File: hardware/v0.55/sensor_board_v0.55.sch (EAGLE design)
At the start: 58 parts, among them J3 USB-MICROB, J6 AVR_SPI_PRG_6PTH, U1 ATMEGA328P, U10 TSL2591, U2 SHT35, U3 OPA344, U5 FT231XS, U6 ADMP401, U7 RFM69HCW, U8 MCP1703CB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

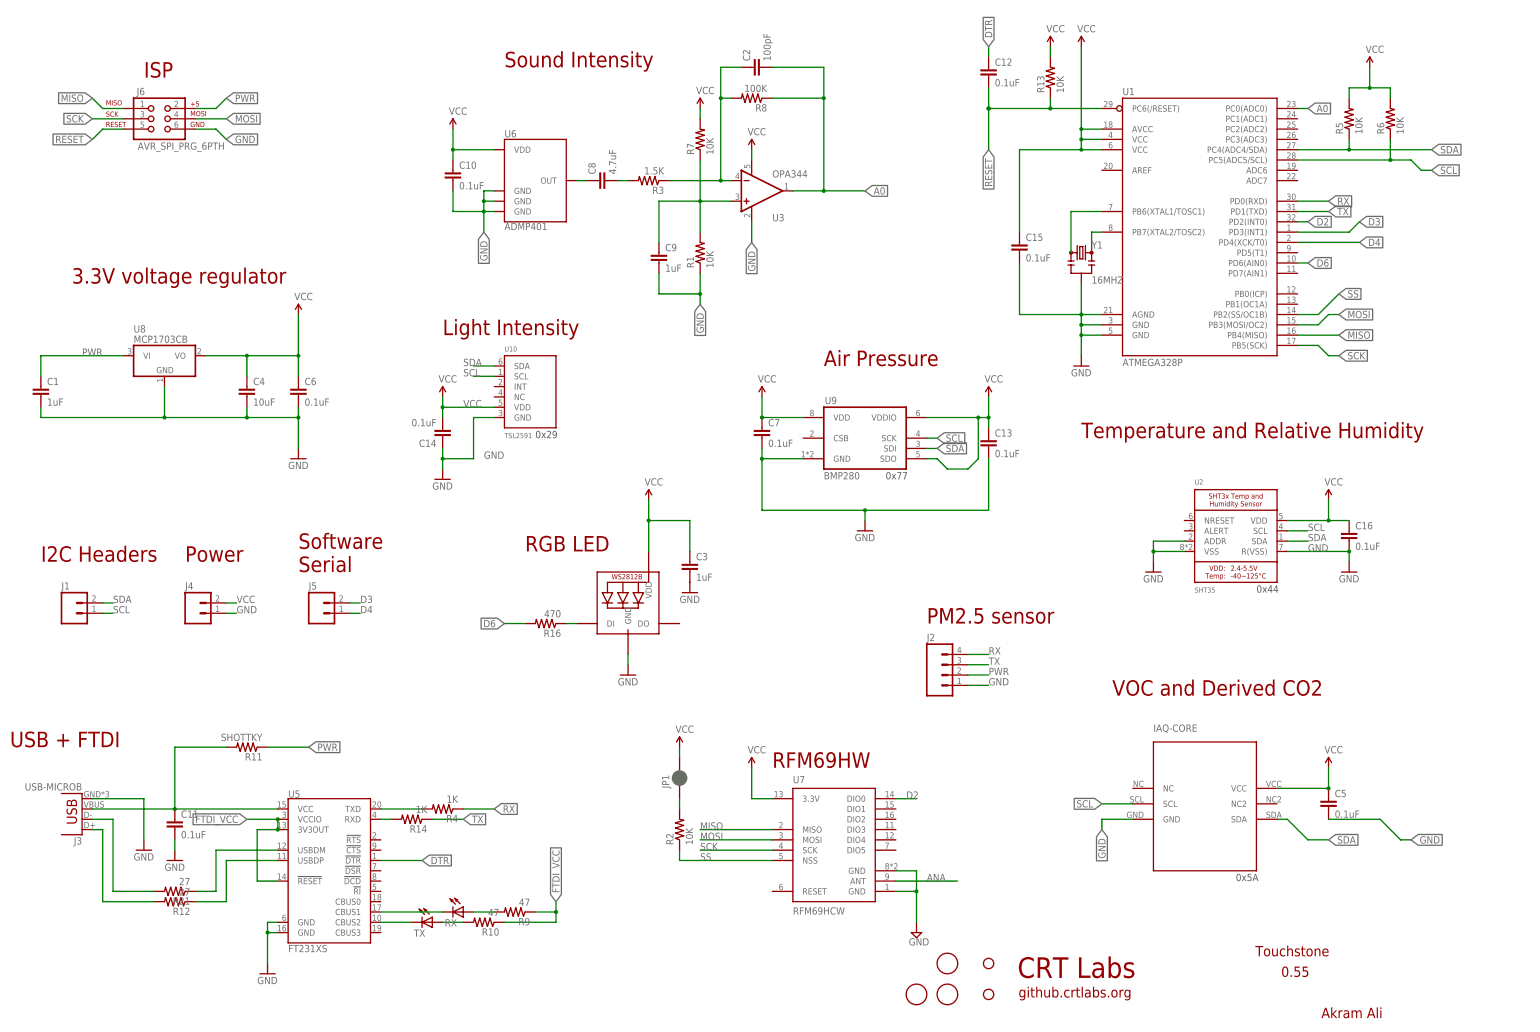
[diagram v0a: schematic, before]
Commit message: v0.55 - Major design update
- Added 2x5 header for PMS7003 PM sensor
- Moved microphone+amp circuitry to accomodate for the PM sensor header
- Removed UART and software serial breakout headers
- Moved voltage regulator circuitry in space created by removing UART
header
- Moved LED in space created by moving voltage regulator
- Moved light sensor to be in line with LED
- Rerouted several traces to accomodate for new design
- Some silkscreen adjustments
- Provided some more tolerance to the mounting holes
- Moved fiducial markers
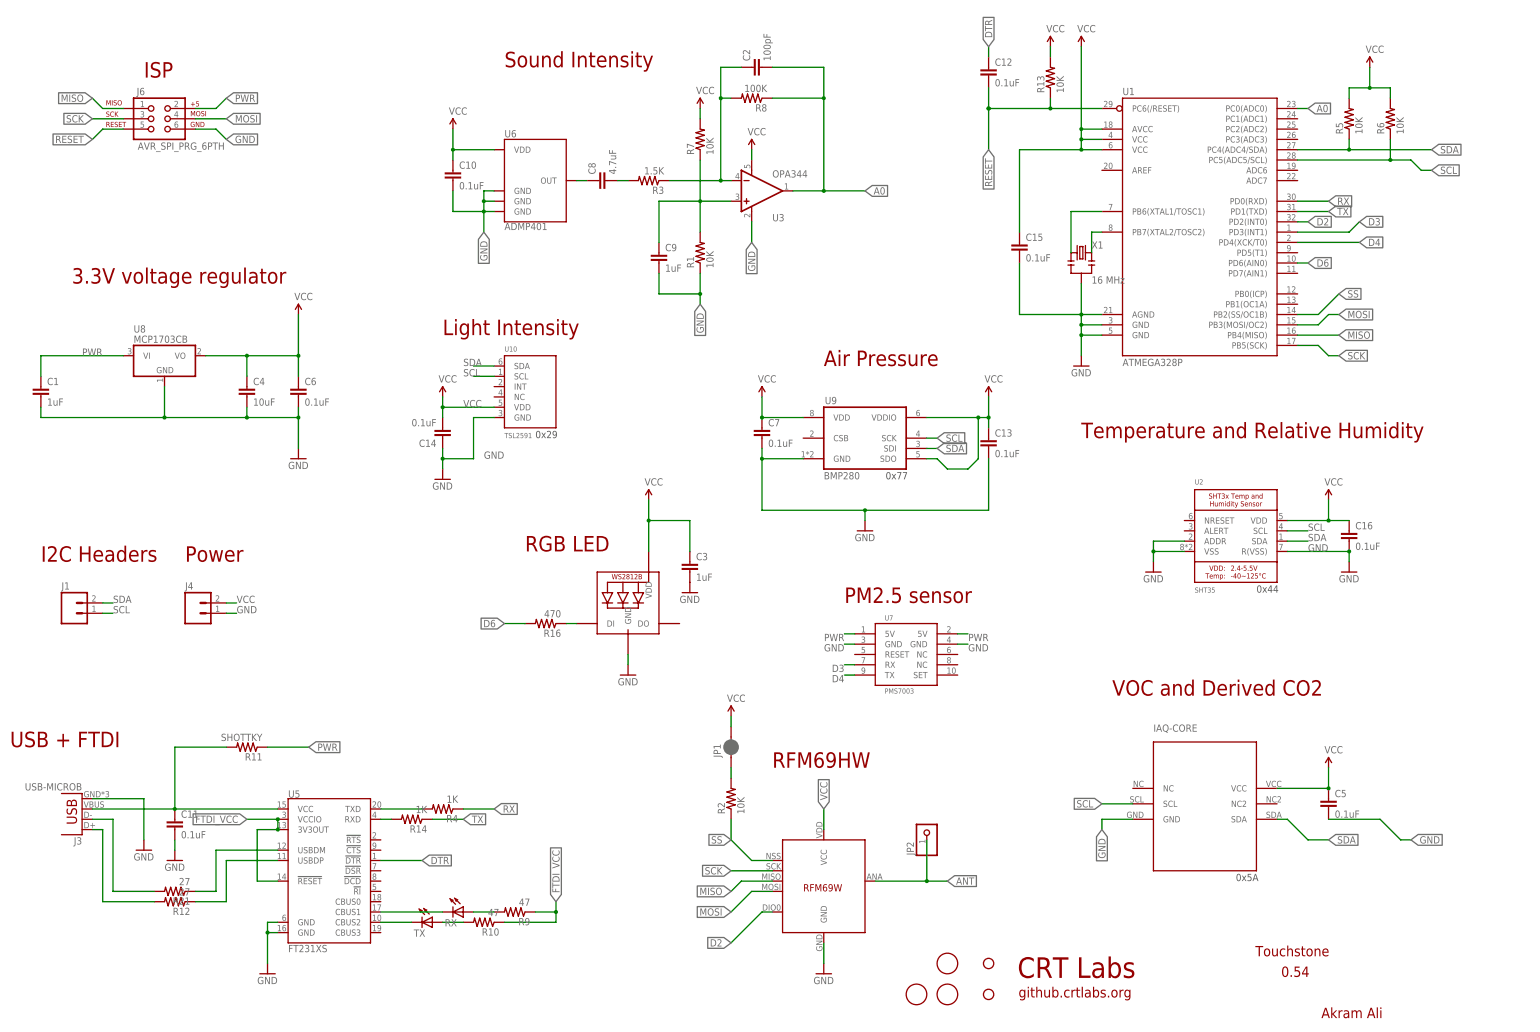
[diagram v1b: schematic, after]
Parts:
- removed J2: (no value), SparkFun-Connectors:M04PTH
- removed J5: (no value), SparkFun-Connectors:M02PTH
- removed Y1: 16MHZ, SparkFun-FreqCtrl:RESONATOR16MHZ
- added JP2: (no value), adafruit:PINHD-1X1
- added U4: RFM69HW, RFM69 USB Gateway:LOWPOWERLAB_RFM69
- added X1: 16 MHz, SparkFun:RESONATORSMD
- U7: value RFM69HCW -> PMS7003; device SparkFun-RF:RFM69HCW -> Amphenol:PMS7003; MPN RFM69HW -> (none)
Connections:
- removed net ANA: U7.ANT
- new net ANT: JP2.1, U4.ANT
- net D2: now also U4.DIO0; no longer U7.DIO0
- net D3: now also U7.RX; no longer J5.2
- net D4: now also U7.TX; no longer J5.1
- net GND: now also U4.GND, U7.GND@0, X1.2; no longer J2.1, U7.GND@2, Y1.2
- net MISO: now also U4.MISO; no longer U7.MISO
- net MOSI: now also U4.MOSI; no longer U7.MOSI
- net N$4: now also X1.3; no longer Y1.3
- net N$5: now also X1.1; no longer Y1.1
- net PWR: now also U7.5V@0, U7.5V@1; no longer J2.2
- net RX: no longer J2.4
- net SCK: now also U4.SCK; no longer U7.SCK
- net SS: now also U4.SEL; no longer U7.NSS
- net TX: no longer J2.3
- net VCC: now also U4.VCC; no longer U7.3.3V
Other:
- note added: "0.54"
- note removed: "0.55"
- note removed: "Software Serial"
- moved on the sheet: JP1, R2

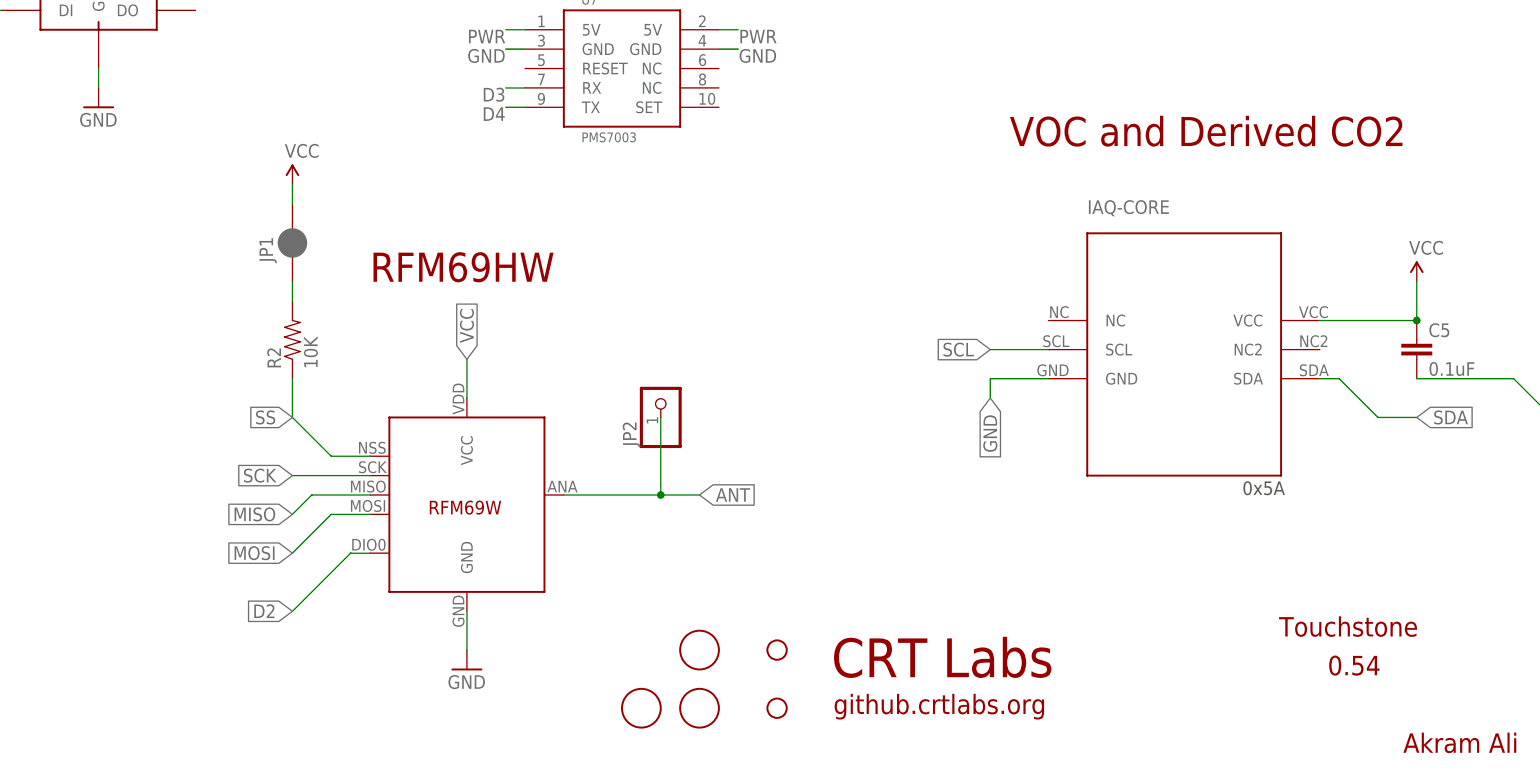
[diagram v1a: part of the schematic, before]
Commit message: v0.55 - major update 2
- Added 915MHz chip antenna (JT 0868AT43A0020E) using ref. designs from:
https://www.johansontechnology.com/datasheets/antennas/0868AT43A0020.pdf
and http://www.ti.com/lit/an/swra160b/swra160b.pdf
- Replaced RFM69HW with RFM69HCW to accomodate for space for chip
antenna
- Rerouted traces to accomodate for new parts
- Adjusted silkscreen
- Minor adjustments to board dimensions (slight increase along Y axis)
- Other minor adjustments to traces, vias, silkscreen
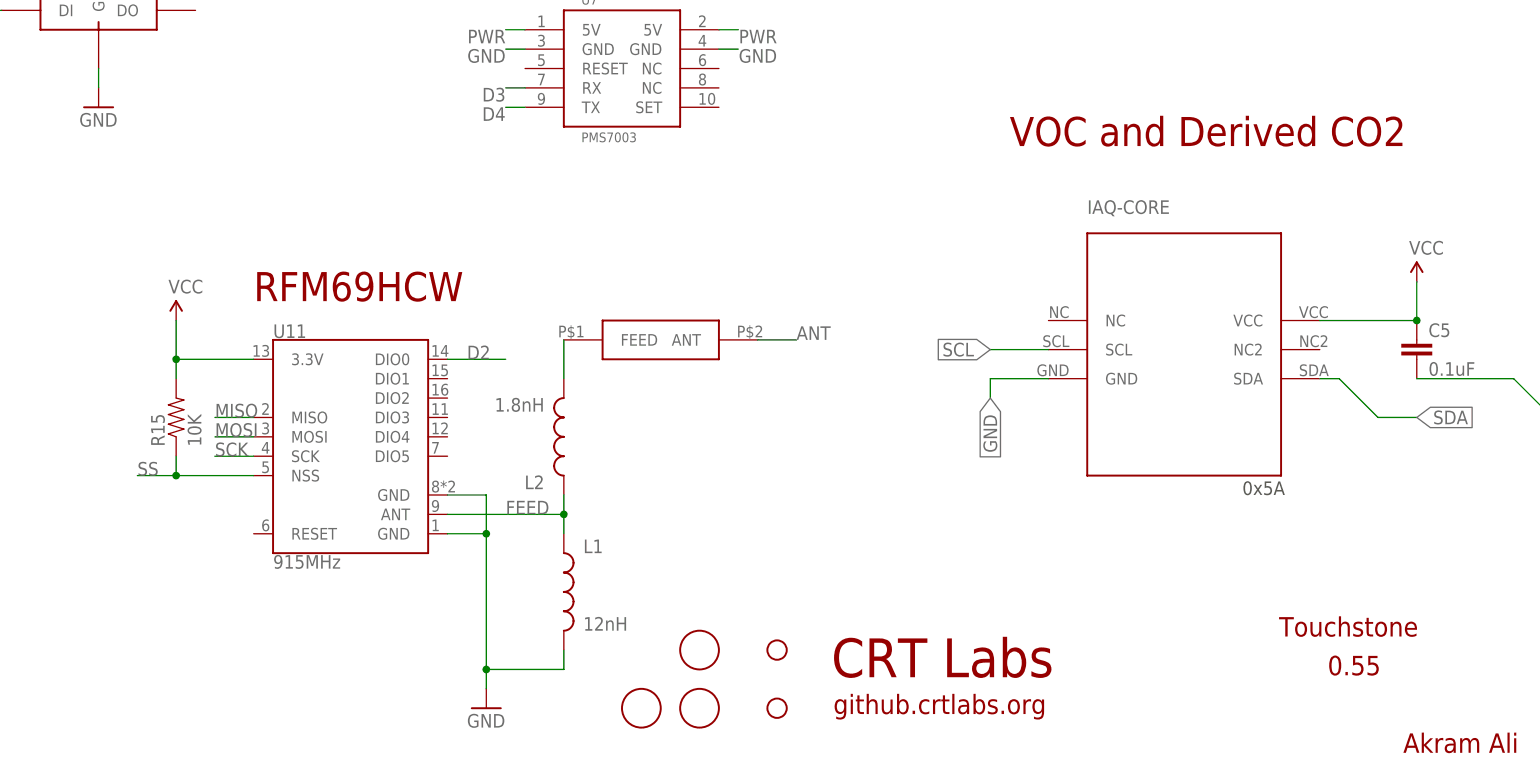
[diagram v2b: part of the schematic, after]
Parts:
- removed JP1: JUMPER-PAD-2-NC_BY_PASTEFULL-BOX-SILK, SparkFun-Passives:JUMPER-PAD-2-NC_BY_PASTEFULL-BOX-SILK
- removed JP2: (no value), adafruit:PINHD-1X1
- removed R2: 10K, SparkFun-Passives:RESISTOR0805-RES
- removed U4: RFM69HW, RFM69 USB Gateway:LOWPOWERLAB_RFM69
- added L1: 12nH, SparkFun-Passives:INDUCTOR0805-IND
- added L2: 1.8nH, SparkFun-Passives:INDUCTOR0805-IND
- added R15: 10K, SparkFun-Passives:RESISTOR0805-RES
- added U$4: 0868AT43A0020E, johanson-technology:0868AT43A0020E
- added U11: 915MHz, SparkFun-RF:RFM69HCW-915
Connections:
- new net FEED: L1.1, L2.1, U11.ANT
- net ANT: now also U$4.ANT; no longer JP2.1, U4.ANT
- net D2: now also U11.DIO0; no longer U4.DIO0
- net GND: now also L1.2, U11.GND@1, U11.GND@2; no longer U4.GND
- net MISO: now also U11.MISO; no longer U4.MISO
- net MOSI: now also U11.MOSI; no longer U4.MOSI
- net N$1: now also L2.2, U$4.FEED; no longer JP1.1, R2.2
- net SCK: now also U11.SCK; no longer U4.SCK
- net SS: now also R15.1, U11.NSS; no longer R2.1, U4.SEL
- net VCC: now also R15.2, U11.3.3V; no longer JP1.2, U4.VCC
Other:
- note added: "0.55"
- note added: "RFM69HCW"
- note removed: "0.54"
- note removed: "RFM69HW"

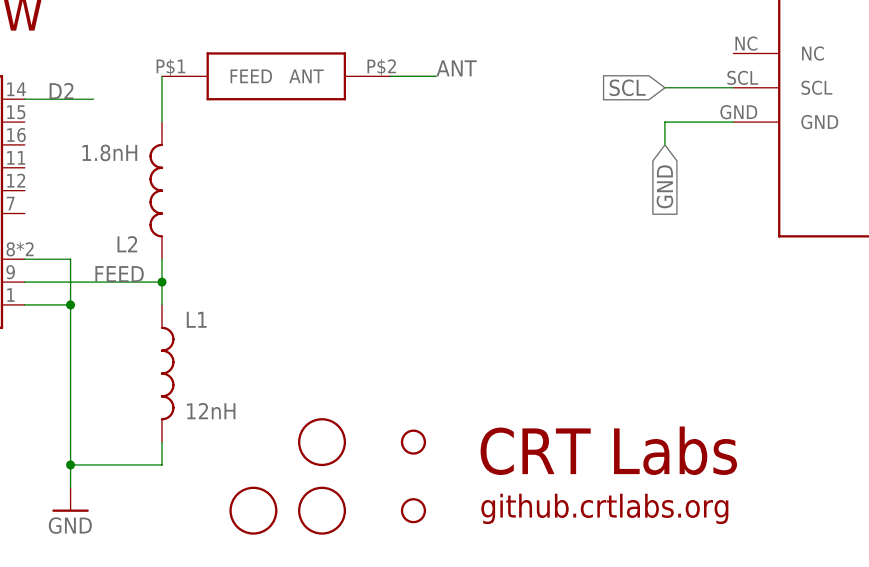
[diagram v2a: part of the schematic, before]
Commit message: Added trace for wire monopole antenna
- wire antenna can be used by means of a jumper (in the event that chip
antenna doesn't work - make sure to desolder the chip antenna +
components)
- not sure of performance of chip + wire antenna trace (with
disconnected jumper) - maybe the trace adds capacitance or random noise?
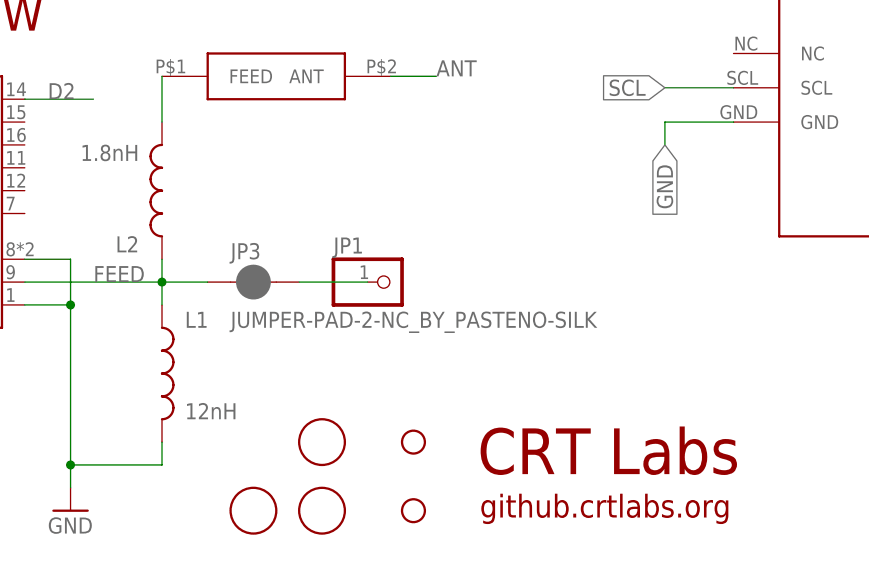
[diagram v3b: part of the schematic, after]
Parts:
- added JP1: (no value), adafruit:PINHD-1X1
- added JP3: JUMPER-PAD-2-NC_BY_PASTENO-SILK, SparkFun-Passives:JUMPER-PAD-2-NC_BY_PASTENO-SILK
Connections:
- new net N$6: JP1.1, JP3.2
- net FEED: now also JP3.1
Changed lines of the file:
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@@
 <part name="L1" library="SparkFun-Passives" deviceset="INDUCTOR" device="0805-IND" value="12nH"/>
 <part name="L2" library="SparkFun-Passives" deviceset="INDUCTOR" device="0805-IND" value="1.8nH"/>
+<part name="JP1" library="adafruit" deviceset="PINHD-1X1" device=""/>
+<part name="JP3" library="SparkFun-Passives" deviceset="JUMPER-PAD-2-NC_BY_PASTE" device="NO-SILK"/>
 </parts>
 <sheets>
@@
 <instance part="L1" gate="G$1" x="157.48" y="-91.44"/>
 <instance part="L2" gate="G$1" x="157.48" y="-71.12" rot="R180"/>
+<instance part="JP1" gate="G$1" x="182.88" y="-81.28"/>
+<instance part="JP3" gate="G$1" x="167.64" y="-81.28"/>
 </instances>
 <busses>
@@
 <wire x1="157.48" y1="-81.28" x2="157.48" y2="-83.82" width="0.1524" layer="91"/>
 <junction x="157.48" y="-81.28"/>
+<wire x1="157.48" y1="-81.28" x2="162.56" y2="-81.28" width="0.1524" layer="91"/>
+<pinref part="JP3" gate="G$1" pin="1"/>
 </segment>
 </net>
@@
 </segment>
 </net>
+<net name="N$6" class="0">
+<segment>
+<pinref part="JP1" gate="G$1" pin="1"/>
+<wire x1="172.72" y1="-81.28" x2="180.34" y2="-81.28" width="0.1524" layer="91"/>
+<pinref part="JP3" gate="G$1" pin="2"/>
+</segment>
+</net>
